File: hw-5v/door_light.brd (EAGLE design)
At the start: 32.2 x 34.6 mm, 30 parts, among them IC1 TINY13-20SSU, Q1 BSP250, T1 n-mosfet, T2 KP-3216P3C, U1 MC33063ADE4

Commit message: fixed few not-so-bright-namings on the schemas
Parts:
- F1: value SD075-16 (F750mA) -> F750mA
- T1: value n-mosfet -> IRFML8244
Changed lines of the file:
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@@
 <attribute name="OC_FARNELL" value="1053588" x="34.02" y="60.96" size="1.778" layer="27" display="off"/>
 </element>
-<element name="F1" library="rcl" package="MINI_MELF-0204W" value="SD075-16 (F750mA)" x="42.53" y="58.41" rot="R180"/>
+<element name="F1" library="rcl" package="MINI_MELF-0204W" value="F750mA" x="42.53" y="58.41" rot="R180"/>
 <element name="R7" library="rcl" package="R0402" value="10kR" x="23.9" y="54.39" rot="R180"/>
 <element name="D1" library="diode" package="SMB" value=" MBRS140T3G" x="28.75" y="68.04"/>
@@
 </element>
 <element name="Q1" library="transistor-fet" package="SOT223" value="BSP250" x="37" y="52"/>
-<element name="T1" library="zetex" package="SOT-23" value="n-mosfet" x="40" y="44" rot="R90">
+<element name="T1" library="zetex" package="SOT-23" value="IRFML8244" x="40" y="44" rot="R90">
 <attribute name="OC_NEWARK" value="unknown" x="40" y="44" size="1.778" layer="27" rot="R90" display="off"/>
 <attribute name="MPN" value="" x="40" y="44" size="1.778" layer="27" rot="R90" display="off"/>

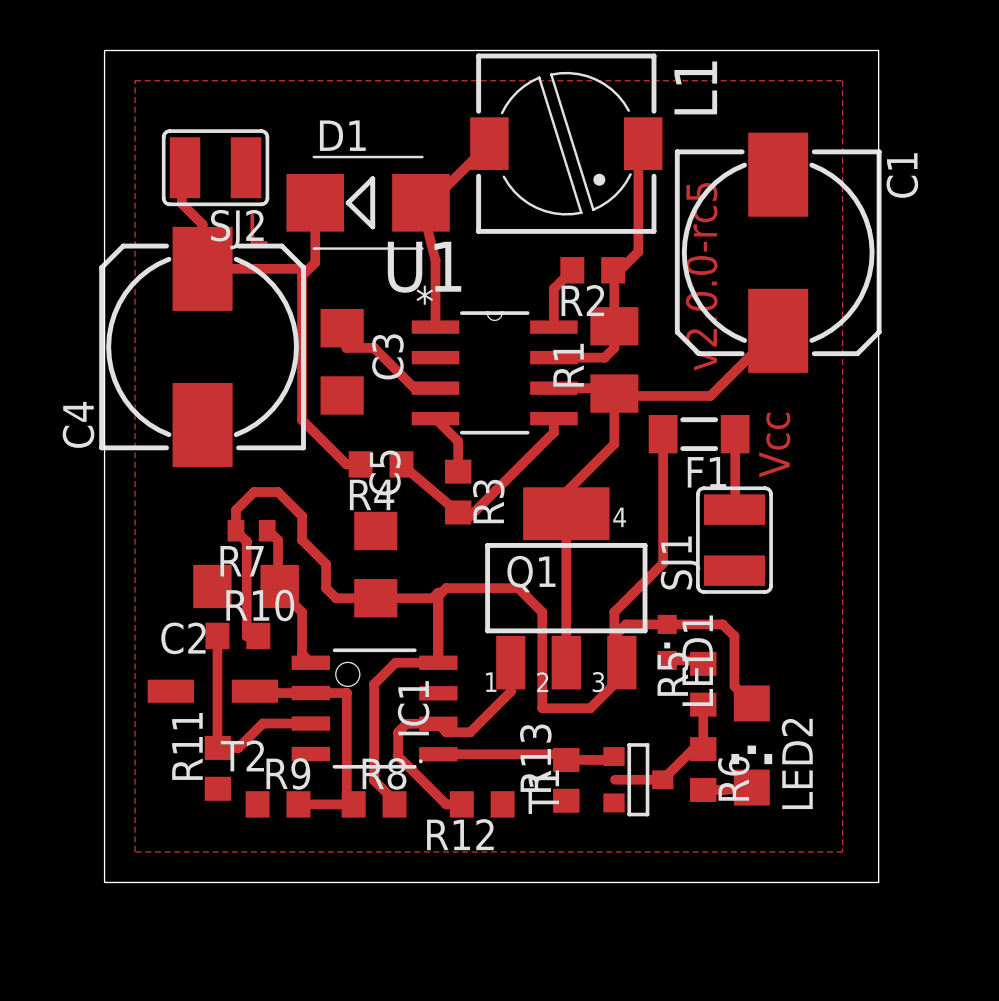
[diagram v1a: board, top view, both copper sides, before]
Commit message: 12V version schema is ready, TODOs fixed; PCB is draft-done - to be tested and improved
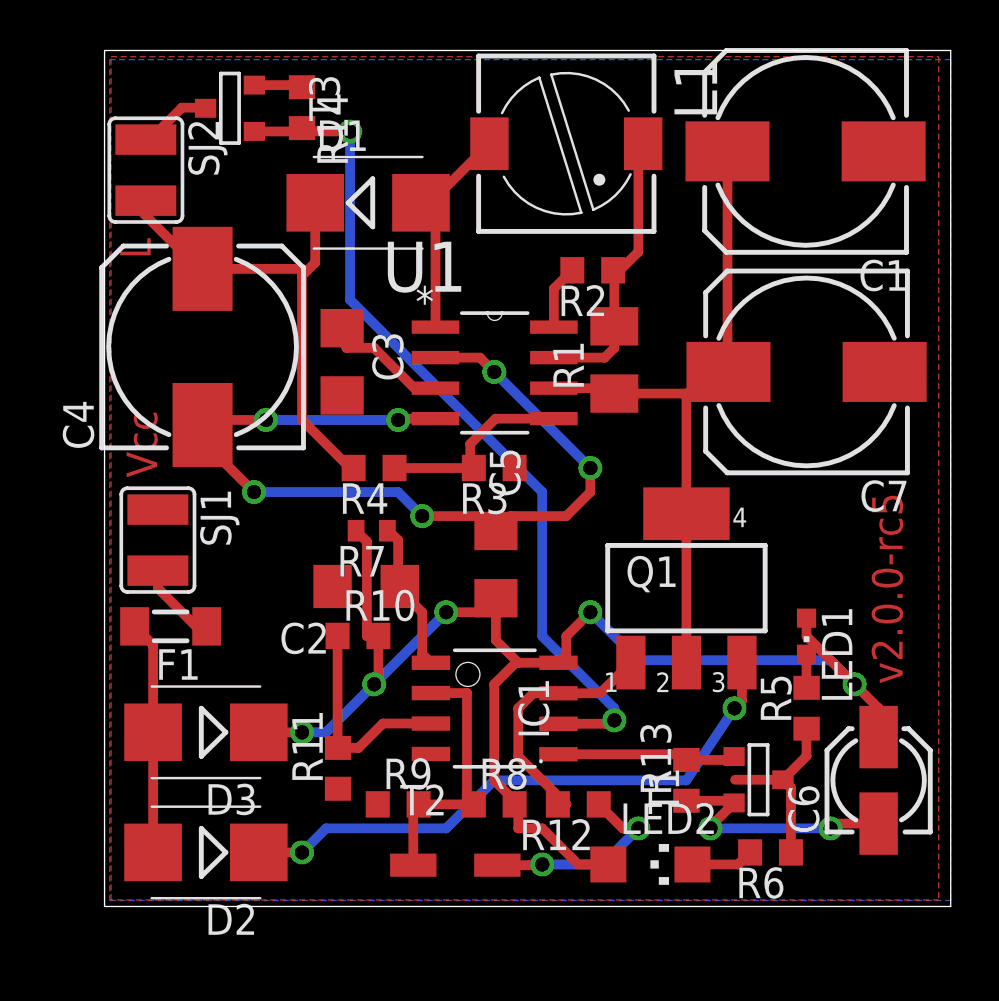
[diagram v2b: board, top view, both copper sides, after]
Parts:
- added C6: 4.7uF, rcl:153CLV-0405
- added C7: 100uF, rcl:153CLV-0810
- added D2, D3: MBRS140T3G, diode:SMB
- added R14: 100kR, rcl:R0603
- added T3: IRFML8244, zetex:SOT-23
- moved SJ1 24.0 mm to (20.0, 54.0), turned to 270 degrees
- moved F1 23.4 mm to (20.5, 50.4)
- moved T2 12.4 mm to (32.0, 40.0), turned to 0 degrees
- moved LED2 6.50 mm to (40.5, 40.5), turned to 270 degrees
- moved LED1 5.81 mm to (47.0, 50.0)
- moved IC1 5.00 mm to (34.0, 47.0)
- moved C2 5.00 mm to (28.7, 52.1)
- moved C5 5.00 mm to (34.1, 53.0)
- moved Q1 5.00 mm to (42.0, 52.0)
- moved R10 5.00 mm to (28.3, 50.0)
- moved R11 5.00 mm to (27.5, 44.5)
- moved R13 5.00 mm to (42.0, 44.0)
- moved R7 5.00 mm to (28.9, 54.4)
- moved R8 5.00 mm to (34.0, 43.0)
- moved R9 5.00 mm to (30.0, 43.0)
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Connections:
- new net N$19: IC1.6, R14.2, T3.3
- new net N$21: D2.A, D3.A, F1.2
- new net N$5: D2.C, Q1.3
- new net N$7: SJ2.1, T3.1
- net +4.1V: now also C6.+, D3.C; no longer F1.2, Q1.3
- net 0V: now also C6.-, C7.-, R14.1, T3.2; no longer SJ2.1
- net N$13: now also IC1.7; no longer IC1.6
- net N$3: now also C7.+
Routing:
- net 0V: track 2.60 -> 59.3 mm, vias 0 -> 10
- net N$19: track 0.00 -> 35.6 mm, vias 0 -> 2
- net N$5: track 0.00 -> 24.7 mm, vias 0 -> 2
- net N$21: track 0.00 -> 9.73 mm
- net +4.1V: track 64.4 -> 57.3 mm, vias 0 -> 5
- net N$3: track 22.6 -> 28.1 mm
- net N$7: track 0.00 -> 3.05 mm
- net N$4: track 6.05 -> 7.69 mm
- net N$18: track 9.15 -> 8.28 mm
- net N$13: track 11.4 -> 10.7 mm
- net N$2: track 2.02 -> 2.61 mm
- added copper zone on layer 16, net 0V
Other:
- board size 32.2 x 34.6 mm -> 35.2 x 35.6 mm

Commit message: route fixes; changed fuse to bigger package (1A)
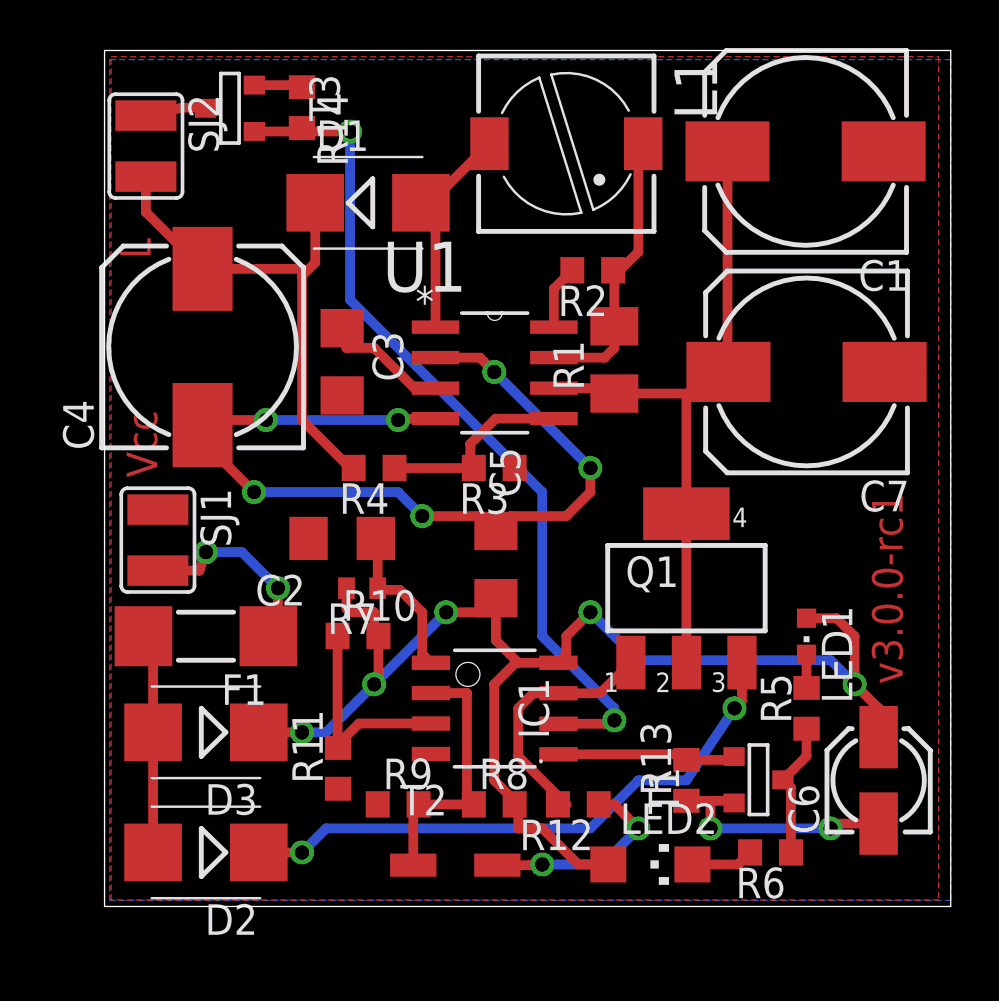
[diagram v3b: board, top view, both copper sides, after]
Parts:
- F1: device rcl:MINI_MELF-0204W -> rcl:MINI_MELF-0207W
- moved R7 2.42 mm to (28.5, 52.0)
- moved C2 2.24 mm to (27.7, 54.1)
- moved F1 1.53 mm to (22.0, 50.0)
- moved SJ2 1.00 mm to (19.5, 70.4)
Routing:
- net N$8: track 3.42 -> 8.33 mm, vias 0 -> 2
- net N$4: track 7.69 -> 5.70 mm
- net +4.1V: track 57.3 -> 56.1 mm
- net N$21: track 9.73 -> 9.18 mm
- net N$7: track 3.05 -> 2.53 mm
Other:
- board text added: "v3.0.0-rc1"
- board text removed: "v2.0.0-rc5"

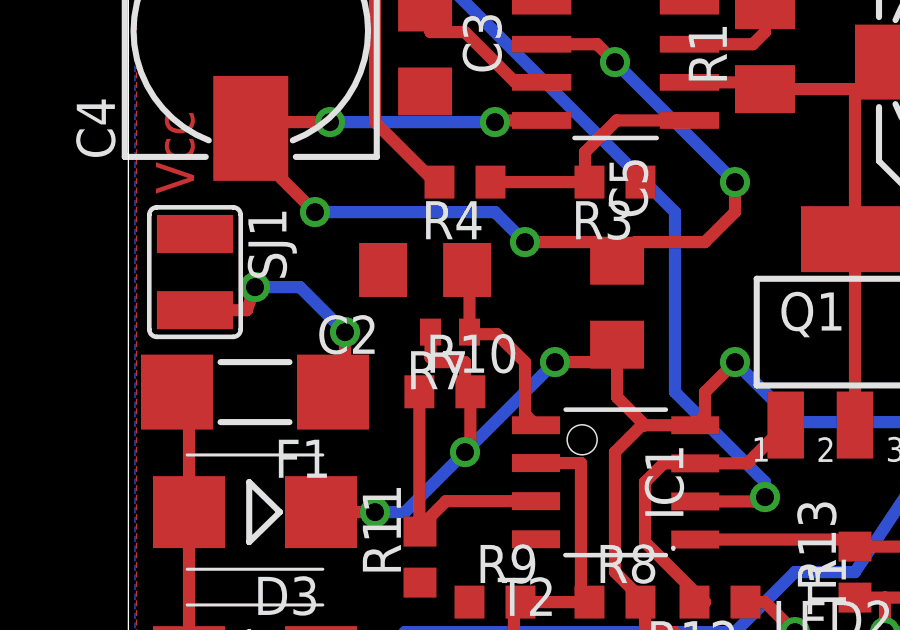
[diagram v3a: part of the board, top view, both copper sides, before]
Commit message: fixed invalid 10kR resistor size
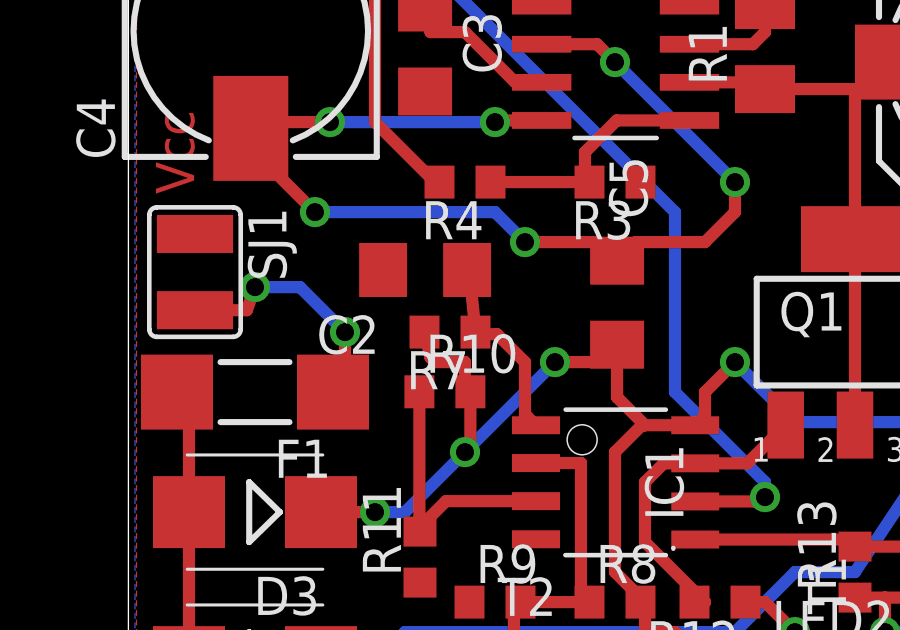
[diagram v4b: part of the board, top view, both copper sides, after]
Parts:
- R7: device rcl:R0402 -> rcl:R0603
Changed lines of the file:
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@@
 </element>
 <element name="F1" library="rcl" package="MINI_MELF-0207W" value="F750mA" x="22" y="50" rot="R180"/>
-<element name="R7" library="rcl" package="R0402" value="10kR" x="28.5" y="52" rot="R180"/>
+<element name="R7" library="rcl" package="R0603" value="10kR" x="28.5" y="52" rot="R180"/>
 <element name="D1" library="diode" package="SMB" value=" MBRS140T3G" x="28.75" y="68.04"/>
 <element name="C3" library="rcl" package="C1206" value="1.5nF" x="27.67" y="61.42" rot="R270"/>
@@
 <wire x1="31" y1="49.261" x2="31.366" y2="48.895" width="0.4064" layer="1"/>
 <wire x1="30.07" y1="51.93" x2="29.22" y2="51.93" width="0.4064" layer="1"/>
-<wire x1="29.22" y1="51.93" x2="29.15" y2="52" width="0.4064" layer="1"/>
-<wire x1="29.15" y1="52" x2="29.15" y2="53.99" width="0.4064" layer="1"/>
+<wire x1="29.22" y1="51.93" x2="29.35" y2="52" width="0.4064" layer="1"/>
+<wire x1="29.35" y1="52" x2="29.15" y2="53.99" width="0.4064" layer="1"/>
 <wire x1="29.15" y1="53.99" x2="29.07" y2="54.07" width="0.4064" layer="1"/>
 </signal>
@@
 <wire x1="47" y1="50.75" x2="48.25" y2="50.75" width="0.4064" layer="1"/>
 <wire x1="48.25" y1="50.75" x2="49" y2="50" width="0.4064" layer="1"/>
-<wire x1="27.85" y1="52" x2="27.85" y2="51.15" width="0.4064" layer="1"/>
+<wire x1="27.65" y1="52" x2="27.85" y2="51.15" width="0.4064" layer="1"/>
 <wire x1="27.85" y1="51.15" x2="28" y2="51" width="0.4064" layer="1"/>
 <wire x1="28" y1="51" x2="29" y2="51" width="0.4064" layer="1"/>
@@
 </signal>
 </signals>
-<errors>
-</errors>
 </board>
 </drawing>

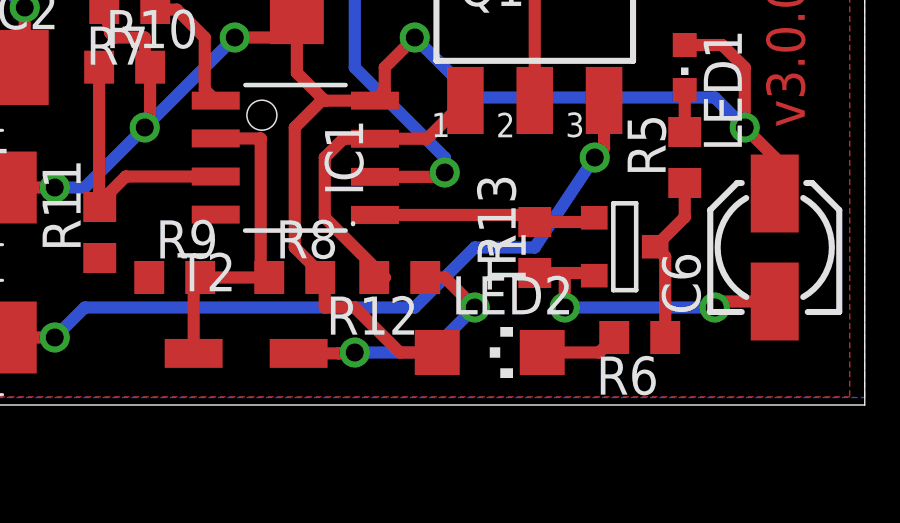
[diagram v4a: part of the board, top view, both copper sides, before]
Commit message: fixed BSP250's pull-down to be a pull-up (10kR)
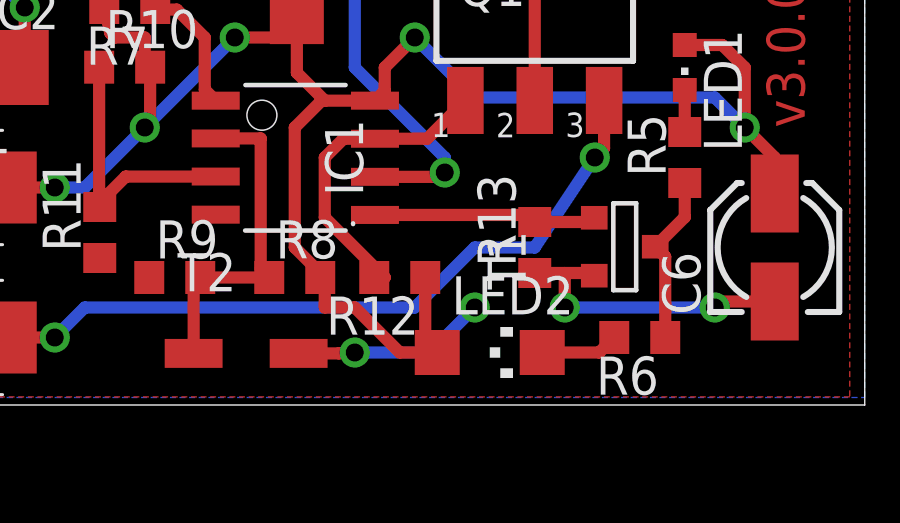
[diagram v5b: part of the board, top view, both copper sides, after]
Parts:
- R12: value 100kR -> 10kR
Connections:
- net +4.1V: now also R12.1
- net 0V: no longer R12.1
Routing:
- net +4.1V: track 56.1 -> 59.0 mm
- net 0V: track 59.0 -> 56.9 mm
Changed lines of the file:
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@@
 <element name="SJ1" library="jumper" package="SJW" value="PWR" x="20" y="54" rot="R270"/>
 <element name="SJ2" library="jumper" package="SJW" value="LIGHT" x="19.5" y="70.4" rot="R270"/>
-<element name="R12" library="rcl" package="R0603" value="100kR" x="37.5" y="43" rot="R180"/>
+<element name="R12" library="rcl" package="R0603" value="10kR" x="37.5" y="43" rot="R180"/>
 <element name="R13" library="rcl" package="R0603" value="100kR" x="42" y="44" rot="R90"/>
 <element name="D2" library="diode" package="SMB" value=" MBRS140T3G" x="22" y="41" rot="R180"/>
@@
 <contactref element="T1" pad="2"/>
 <contactref element="SJ1" pad="1"/>
-<contactref element="R12" pad="1"/>
 <contactref element="R13" pad="1"/>
 <contactref element="C6" pad="-"/>
@@
 <wire x1="37" y1="55" x2="34.69" y2="55" width="0.4064" layer="1"/>
 <wire x1="34.69" y1="55" x2="34.07" y2="54.38" width="0.4064" layer="1"/>
-<wire x1="38.35" y1="43" x2="39" y2="43" width="0.4064" layer="1"/>
-<wire x1="39" y1="43" x2="40" y2="42" width="0.4064" layer="1"/>
 <wire x1="43" y1="42" x2="43" y2="43.15" width="0.4064" layer="1"/>
 <wire x1="21.86" y1="58.14" x2="24" y2="56" width="0.4064" layer="1"/>
@@
 <wire x1="29" y1="51" x2="29" y2="50.19" width="0.4064" layer="1"/>
 <wire x1="29" y1="50.19" x2="29.18" y2="50.01" width="0.4064" layer="1"/>
+<contactref element="R12" pad="1"/>
+<wire x1="38.75" y1="40.5" x2="38.35" y2="40.5" width="0.4064" layer="1"/>
+<wire x1="38.35" y1="40.5" x2="38.35" y2="43" width="0.4064" layer="1"/>
 </signal>
 <signal name="N$10">

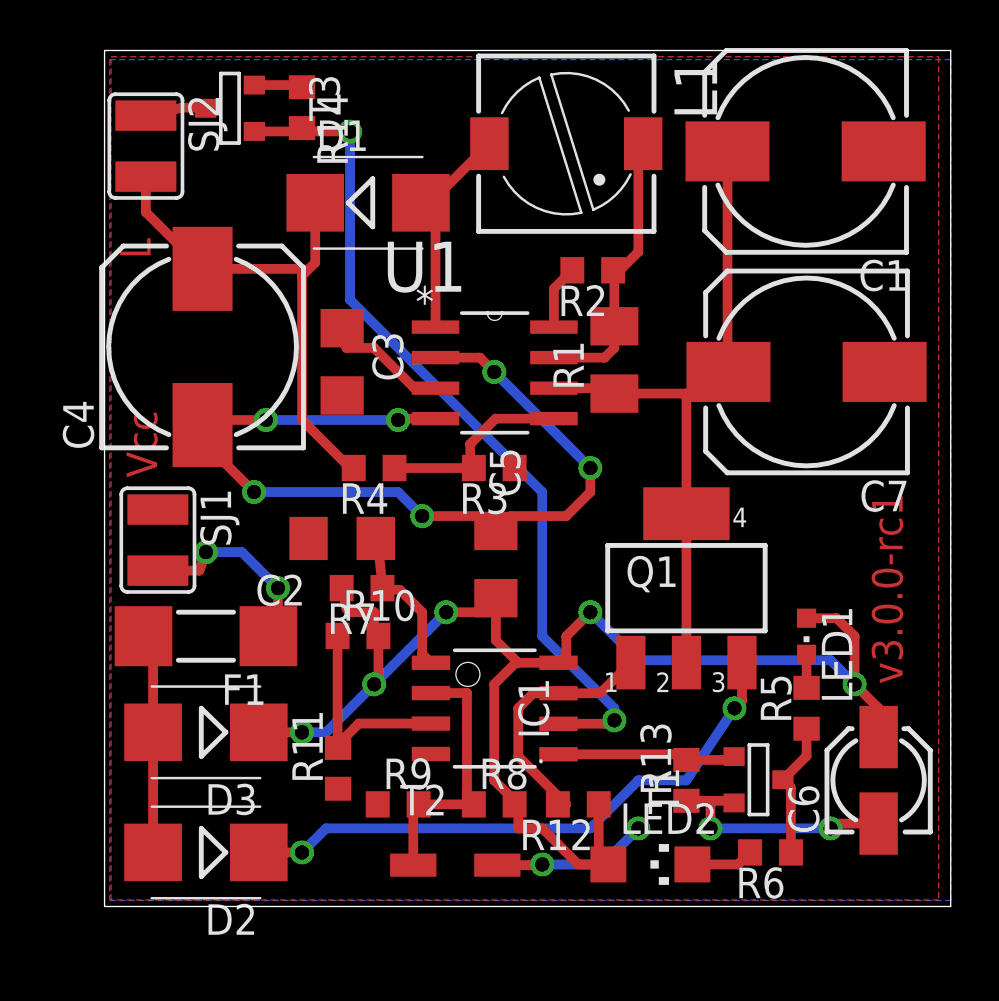
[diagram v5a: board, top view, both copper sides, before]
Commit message: added -3V zenner for ensuring reasonable measurements of IR light change
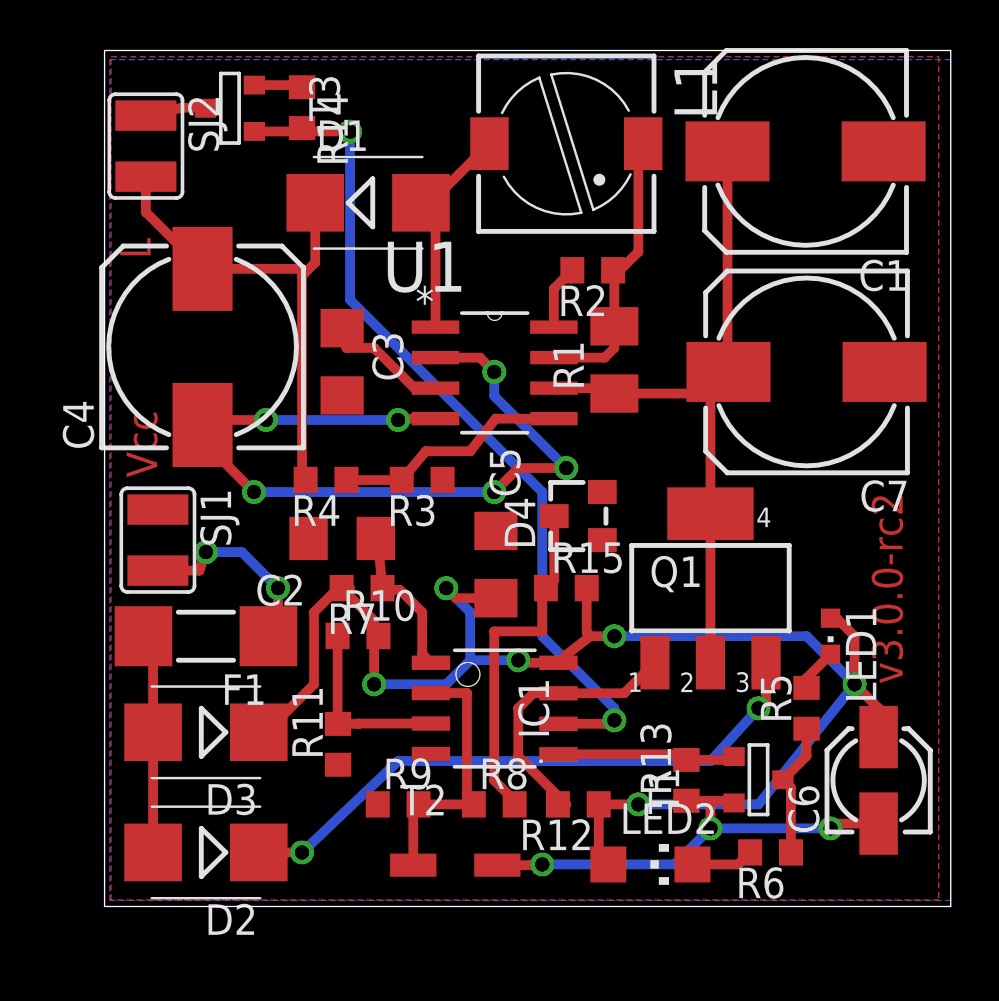
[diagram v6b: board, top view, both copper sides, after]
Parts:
- added D4: BZX84C3V0 (-3V), diode:TO236
- added R15: 5.1kR, rcl:R0603
- R8: value 10kR -> 5.1kR
- moved R3 3.04 mm to (31.0, 56.5)
- moved R4 2.06 mm to (27.0, 56.5)
- moved LED1 1.00 mm to (48.0, 50.0)
- moved Q1 1.00 mm to (43.0, 52.0)
- moved R11 1.00 mm to (27.5, 45.5)
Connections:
- new net N$6: D4.C, R15.1, R8.2
- net +4.1V: now also R15.2; no longer R8.2
- net 0V: now also D4.A
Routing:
- net N$6: track 0.00 -> 14.6 mm
- net +4.1V: track 59.0 -> 65.7 mm, vias 5 -> 6
- net N$17: track 9.25 -> 7.54 mm
- net N$18: track 8.28 -> 9.86 mm
- net N$13: track 10.7 -> 11.7 mm
- net N$5: track 24.7 -> 25.3 mm
- net 0V: track 56.9 -> 57.5 mm, vias 10 -> 9
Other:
- board text added: "v3.0.0-rc2"
- board text removed: "v3.0.0-rc1"
